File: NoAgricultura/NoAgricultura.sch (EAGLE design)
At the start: 16 parts, among them IC1 PIC18F45K80-I_PT, U1 MCP73832T-5ACI/OT

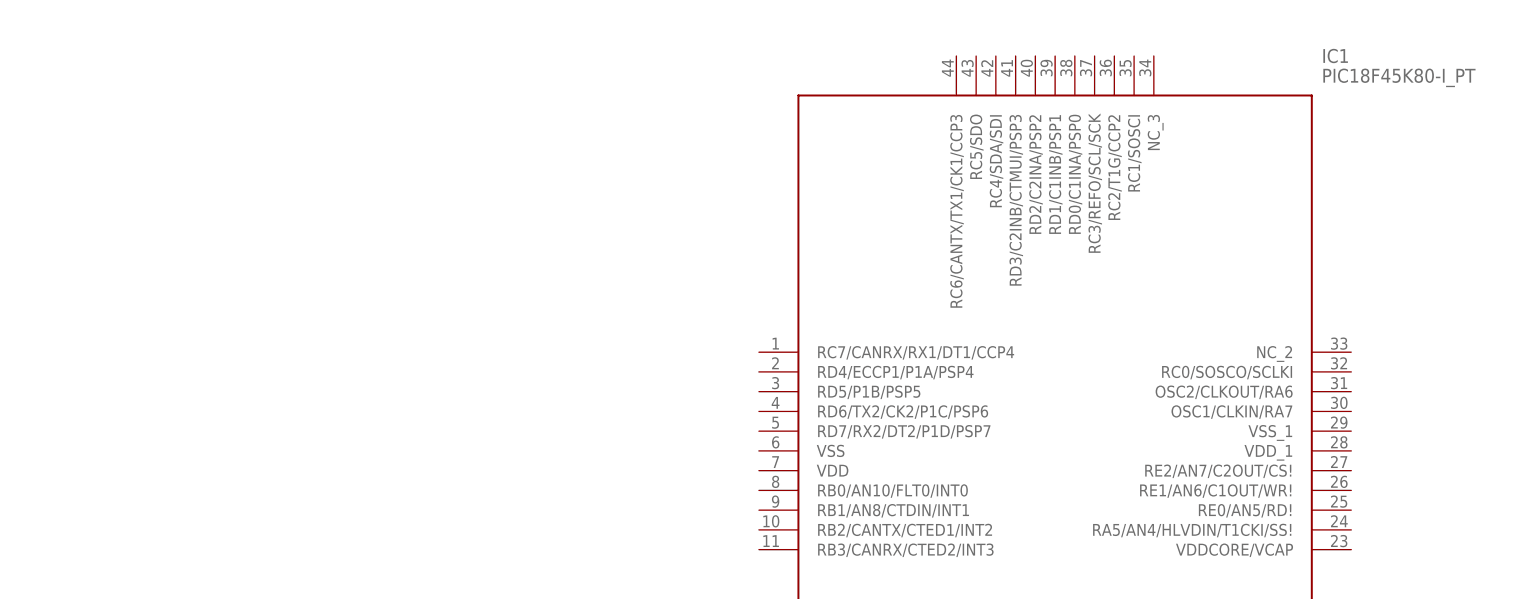
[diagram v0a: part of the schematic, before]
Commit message: Circuito MCLR
Componentes baixados e circuito montado.
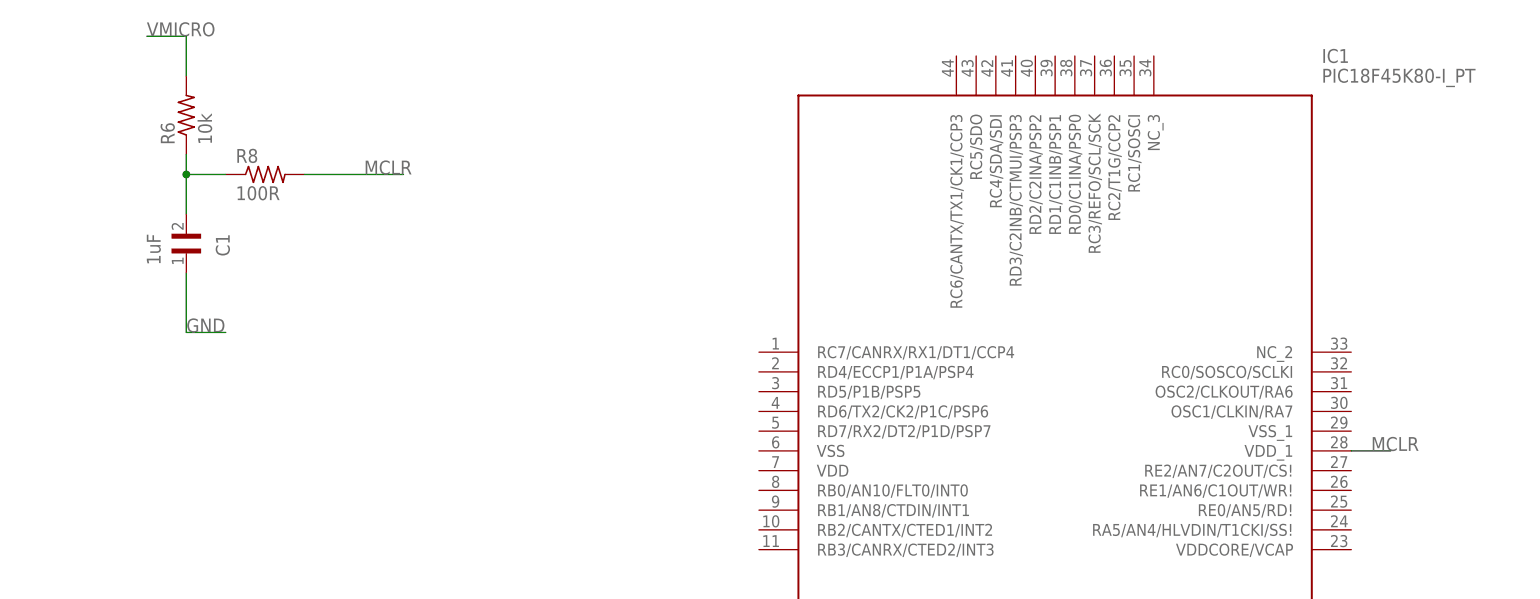
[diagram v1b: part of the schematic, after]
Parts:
- added C1: 1uF, 0805YC104KA76A:0805YC104KA76A
- added R6: 10k, 0805 Resistor:CRGH0805F392R
- added R8: 100R, 0805 Resistor:CRGH0805F392R
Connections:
- new net MCLR: IC1.VDD_1, R8.2
- new net N$7: C1.2, R6.1, R8.1
- new net VMICRO: R6.2
- net GND: now also C1.1
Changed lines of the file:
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@@
 <part name="U$7" library="CAPTANT-TYPEA" deviceset="CAPTANT-TYPEA" device="" package3d_urn="urn:adsk.eagle:package:10697356/1"/>
 <part name="IC1" library="PIC18F45K80-I_PT" deviceset="PIC18F45K80-I_PT" device=""/>
+<part name="C1" library="0805YC104KA76A" deviceset="0805YC104KA76A" device="" value="1uF"/>
+<part name="R6" library="0805 Resistor" library_urn="urn:adsk.eagle:library:10617584" deviceset="CRGH0805F392R" device="" package3d_urn="urn:adsk.eagle:package:10617587/1" value="10k"/>
+<part name="R8" library="0805 Resistor" library_urn="urn:adsk.eagle:library:10617584" deviceset="CRGH0805F392R" device="" package3d_urn="urn:adsk.eagle:package:10617587/1" value="100R"/>
 </parts>
 <sheets>
@@
 <attribute name="VALUE" x="392.43" y="261.62" size="1.778" layer="96" align="center-left"/>
 </instance>
+<instance part="C1" gate="G$1" x="246.38" y="241.3" smashed="yes" rot="R270">
+<attribute name="NAME" x="250.19" y="241.3" size="1.778" layer="95" rot="R270"/>
+<attribute name="VALUE" x="241.3" y="241.3" size="1.778" layer="96" rot="R270"/>
+</instance>
+<instance part="R6" gate="G$1" x="246.38" y="256.54" smashed="yes" rot="R90">
+<attribute name="NAME" x="244.8814" y="252.73" size="1.778" layer="95" rot="R90"/>
+<attribute name="VALUE" x="249.682" y="252.73" size="1.778" layer="96" rot="R90"/>
+</instance>
+<instance part="R8" gate="G$1" x="256.54" y="248.92" smashed="yes">
+<attribute name="NAME" x="252.73" y="250.4186" size="1.778" layer="95"/>
+<attribute name="VALUE" x="252.73" y="245.618" size="1.778" layer="96"/>
+</instance>
 </instances>
 <busses>
@@
 <pinref part="U$7" gate="G$1" pin="-"/>
 </segment>
-</net>
+<segment>
+<pinref part="C1" gate="G$1" pin="1"/>
+<wire x1="246.38" y1="236.22" x2="246.38" y2="228.6" width="0.1524" layer="91"/>
+<wire x1="246.38" y1="228.6" x2="251.46" y2="228.6" width="0.1524" layer="91"/>
+<label x="246.38" y="228.6" size="1.778" layer="95"/>
+</segment>
+</net>
+<net name="VMICRO" class="0">
+<segment>
+<pinref part="R6" gate="G$1" pin="2"/>
+<wire x1="246.38" y1="261.62" x2="246.38" y2="266.7" width="0.1524" layer="91"/>
+<wire x1="246.38" y1="266.7" x2="241.3" y2="266.7" width="0.1524" layer="91"/>
+<label x="241.3" y="266.7" size="1.778" layer="95"/>
+</segment>
+</net>
+<net name="N$7" class="0">
+<segment>
+<pinref part="R6" gate="G$1" pin="1"/>
+<pinref part="C1" gate="G$1" pin="2"/>
+<wire x1="246.38" y1="251.46" x2="246.38" y2="248.92" width="0.1524" layer="91"/>
+<pinref part="R8" gate="G$1" pin="1"/>
+<wire x1="246.38" y1="248.92" x2="246.38" y2="243.84" width="0.1524" layer="91"/>
+<wire x1="246.38" y1="248.92" x2="251.46" y2="248.92" width="0.1524" layer="91"/>
+<junction x="246.38" y="248.92"/>
+</segment>
+</net>
+<net name="MCLR" class="0">
+<segment>
+<pinref part="R8" gate="G$1" pin="2"/>
+<wire x1="261.62" y1="248.92" x2="274.32" y2="248.92" width="0.1524" layer="91"/>
+<label x="269.24" y="248.92" size="1.778" layer="95"/>
+</segment>
+<segment>
+<pinref part="IC1" gate="G$1" pin="VDD_1"/>
+<wire x1="396.24" y1="213.36" x2="401.32" y2="213.36" width="0.1524" layer="91"/>
+<label x="398.78" y="213.36" size="1.778" layer="95"/>
+</segment>
+</net>

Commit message: Sensores de Umidade
Adicionado circuito dos sensores e de Gravação inCircuit
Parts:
- added C2, C3, C5, C6: 1uF, 0805YC104KA76A:0805YC104KA76A
- added C4: 10uF, 0805YC104KA76A:0805YC104KA76A
- added D1, D2, D3: 598-8160-107F, led0805:598-8160-107F
- added R10, R9: 10k, 0805 Resistor:CRGH0805F392R
- added R11, R12, R13: 2K, 0805 Resistor:CRGH0805F392R
- added U$8: TEMP-HUM-SENSOR-DHT22, diy-modules:TEMP-HUM-SENSOR-DHT22
- added U$9: CAPTANT-TYPEA, CAPTANT-TYPEA:CAPTANT-TYPEA
- added U3: HTU21D, HTU21D:HTU21D
- added X1, X2: 22-23-2051, con-molex:22-23-2051
- added X3, X4: 22-23-2021, con-molex:22-23-2021
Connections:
- removed net GND: C1.1, R7.2, U$7.-, U1.VSS
- removed net IN-: U$2.D, U$4.D
- removed net VMICRO: R6.2
- new net AN0: IC1.RA0/CVREF/AN0/ULPWU, X2-2.S
- new net ICSPCLK: IC1.RB6/PGC/KBI2, X1-5.S
- new net ICSPDAT: IC1.RB7/PGD/T3G/KBI3, X1-4.S
- new net LED1: D1.A, IC1.RC0/SOSCO/SCLKI
- new net LED2: D2.A, IC1.RC1/SOSCI
- new net LED3: D3.A, IC1.RC2/T1G/CCP2
- new net N$10: C6.2, U3.VDD
- new net N$14: R11.2
- new net N$15: R12.2
- new net N$3: D1.C, R13.1
- new net N$6: IC1.RA3/VREF+/AN3
- new net N$8: D3.C, R11.1
- new net N$9: C6.1, U3.GND
- new net SCL: IC1.RC3/REFO/SCL/SCK, R10.1, U3.SCK, X2-4.S
- new net SDA: IC1.RC4/SDA/SDI, R9.1, U$8.DAT, U3.DATA, X2-3.S
- new net VDD: C4.2, C5.2, IC1.VDDCORE/VCAP, R10.2, R6.2, R9.2, U$5.D, U$6.+, U$7.+, U$8.VDD, U1.VDD, X1-2.S, X2-1.S
- new net VDD_1: C3.1, IC1.VDD_1
- new net VSS: C1.1, C2.1, C2.2, C4.1, C5.1, IC1.VDD, IC1.VSS, R13.2, R7.2, U$2.D, U$4.D, U$6.-, U$7.-, U$8.GND, U$9.-, U1.VSS, X1-3.S, X2-5.S, X3-2.S, X4-2.S
- new net VSS_1: C3.2, IC1.VSS_1
- net IN+: now also X3-1.S
- net MCLR: now also X1-1.S; no longer IC1.VDD_1
- net N$5: now also D2.C, R12.1; no longer U$5.D
- net OUT+: no longer U$7.+, U1.VDD
- net SW1: now also IC1.RA1/AN1/C1INC
- net SW2: now also IC1.RA2/VREF-/AN2/C2INC
- net SW3: now also IC1.RA5/AN4/HLVDIN/T1CKI/SS!
- net SW4: now also IC1.RE0/AN5/RD!
- net SWCAP: now also IC1.RE1/AN6/C1OUT/WR!
- net VBAT: now also U$9.+, X4-1.S
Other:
- note added: "DHT22"
- note added: "Gravação inCircuit"
- note added: "HTU21D"
- note added: "LEDS"
- note added: "MCLR"
- note added: "Sensor de Humidade do Solo"
- moved on the sheet: C1, R6, R8
